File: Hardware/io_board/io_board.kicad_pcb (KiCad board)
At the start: 2 copper layers, 80.8 x 60.1 mm, 35 parts, among them J1 Conn_01x40, J2 Conn_02x06_Odd_Even, J3 Mini-DIN-6, J4 Conn_02x10_Odd_Even, J5 Conn_01x04_Male, U2 W65C22NxP, U3 74LS14, U4 74HC137

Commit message: update for kicad 6
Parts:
- removed the G*** at (39.9, -15.2)
- added G***: LOGO, Logo:logo, F.Cu at (40.3, -15.0)
- moved REF** 33.8 mm to (15.0, -12.3)
- moved REF** 1.17 mm to (8.55, -10.6)
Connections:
- J4 pad 13: unconnected-(J4-Pad13) -> GND
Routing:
- net GND: track 3.85 -> 7.18 mm
- net Net-(D2-Pad1): track 9.24 -> 6.87 mm
- net /PA0: track 43.2 -> 41.1 mm
- net ~{CONF}: track 68.5 -> 66.7 mm
- net /PA2: track 48.8 -> 47.1 mm
- net /PA4: track 49.0 -> 47.3 mm
- net /PA3: track 47.8 -> 46.5 mm
- net +5V: track 12.7 -> 11.9 mm
- net Net-(D8-Pad1): track 9.60 -> 8.84 mm
- net Net-(J3-Pad5): track 30.9 -> 30.1 mm
- net /PA5: track 51.5 -> 50.8 mm
- net ~{RESET}: track 31.3 -> 30.6 mm
- net /PA1: track 48.4 -> 47.8 mm
- net Net-(U3-Pad11): track 3.09 -> 2.54 mm
- net /SS4: track 9.85 -> 9.34 mm
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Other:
- board text added: "IO BOARD ${VERSION}"
- board text removed: "IO BOARD V1.1"
- board text removed: "IO BOARD V1.2"

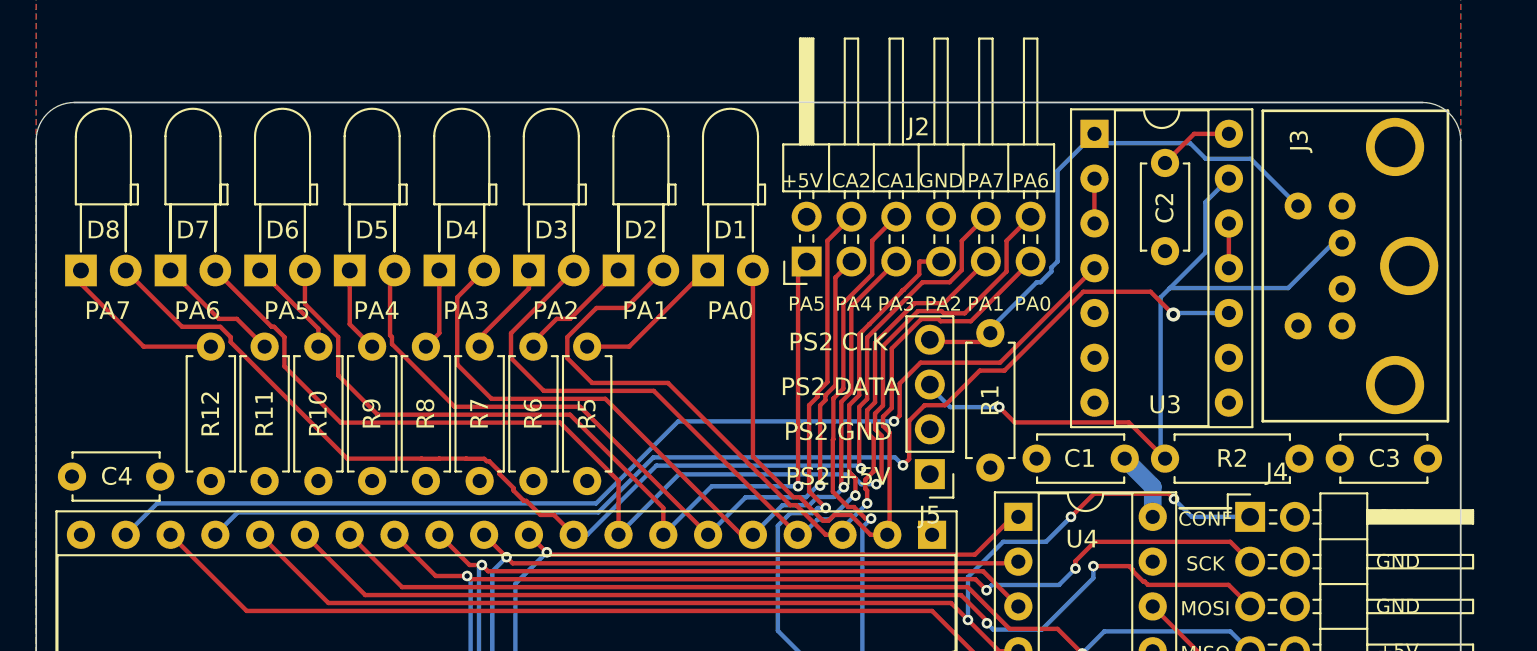
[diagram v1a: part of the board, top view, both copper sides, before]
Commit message: update io board
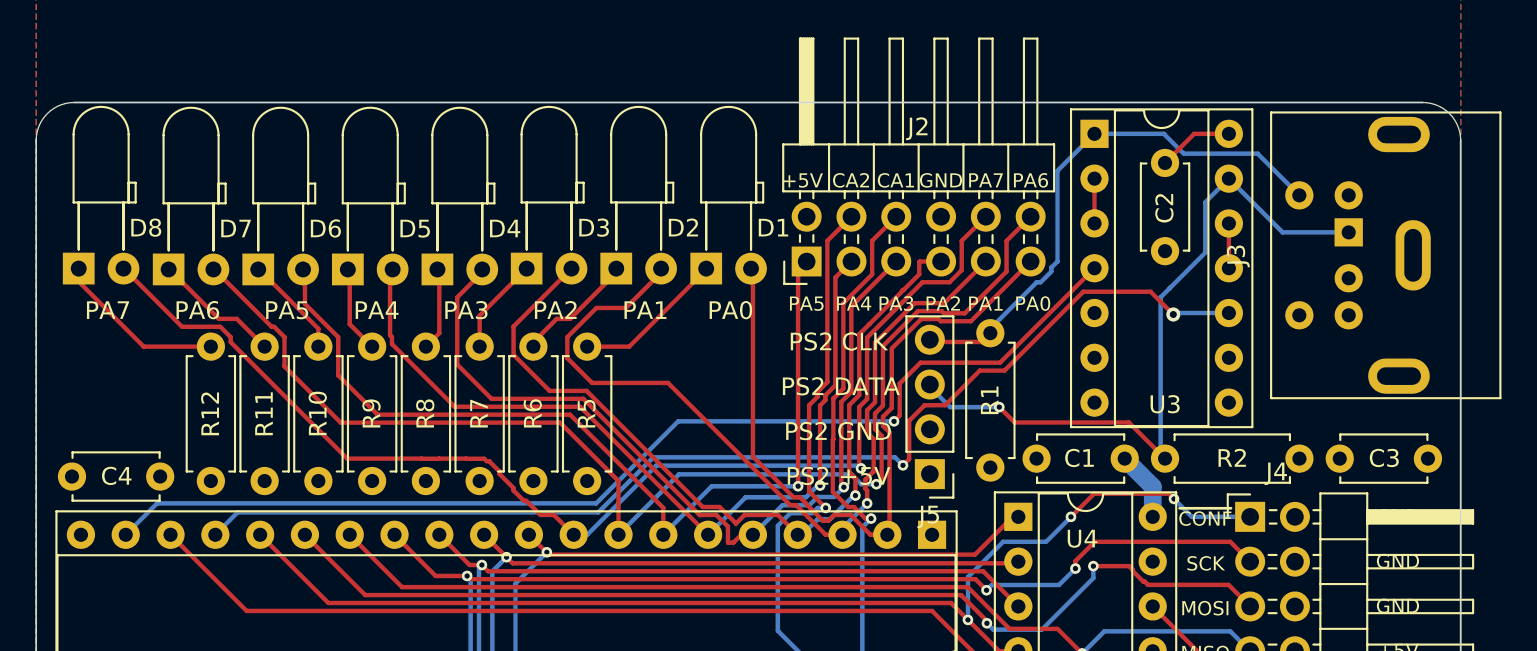
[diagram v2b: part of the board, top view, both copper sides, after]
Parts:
- D1, D2, D3, D4, D5, D6, D7, D8: footprint LED_THT:LED_D3.0mm_Horizontal_O3.81mm_Z6.0mm -> w_conn_av:LED_D3.0mm_Horizontal_O3.81mm_Z6.0mm_2
- J3: footprint mini-din:MINI-DIN-6-FULL-SHIELD -> Custom_Footprints:Connector_Mini-DIN_Female_6Pin_2rows
- moved D3 11.2 mm to (27.8, -60.5), turned to 0 degrees
- moved D1 11.2 mm to (38.0, -60.5), turned to 0 degrees
- moved D4 11.1 mm to (22.8, -60.4), turned to 0 degrees
- moved D8 10.3 mm to (2.41, -60.5), turned to 0 degrees
- moved D5 10.2 mm to (17.7, -60.4), turned to 0 degrees
- moved D7 10.2 mm to (7.51, -60.4), turned to 0 degrees
- moved D2 9.91 mm to (32.9, -60.5), turned to 0 degrees
- moved D6 9.86 mm to (12.6, -60.4), turned to 0 degrees
- moved J3 8.35 mm to (74.4, -52.7), turned to 90 degrees
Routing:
- net PS2_DATA: track 42.9 -> 40.6 mm
- net /PA3: track 46.5 -> 47.4 mm
- net Net-(J3-Pad5): track 30.1 -> 30.7 mm

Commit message: IO board DRC
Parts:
- moved C1 165.5 mm to (142.0, 104.9)
- moved C2 165.5 mm to (144.3, 88.1)
- moved C3 165.5 mm to (154.2, 104.9)
- moved C4 165.5 mm to (82.3, 105.9)
- moved D1 165.5 mm to (118.3, 84.3)
- moved D2 165.5 mm to (113.2, 84.3)
- moved D3 165.5 mm to (108.1, 84.3)
- moved D4 165.5 mm to (103.0, 84.4)
- moved D5 165.5 mm to (97.9, 84.4)
- moved D6 165.5 mm to (92.9, 84.4)
- moved D7 165.5 mm to (87.8, 84.4)
- moved D8 165.5 mm to (82.7, 84.3)
- moved G*** 165.5 mm to (120.5, 129.8)
- moved J1 165.5 mm to (158.5, 138.2)
- moved J2 165.5 mm to (124.0, 93.7)
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
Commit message: cleanup
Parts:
- moved REF** 3.30 mm to (98.6, 132.6)
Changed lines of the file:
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@@
   )
   (footprint "Symbol:OSHW-Logo2_7.3x6mm_SilkScreen" (layer "F.Cu")
-    (at 95.25 132.461)
+    (at 98.552 132.588)
     (descr "Open Source Hardware Symbol")
     (tags "Logo Symbol OSHW")

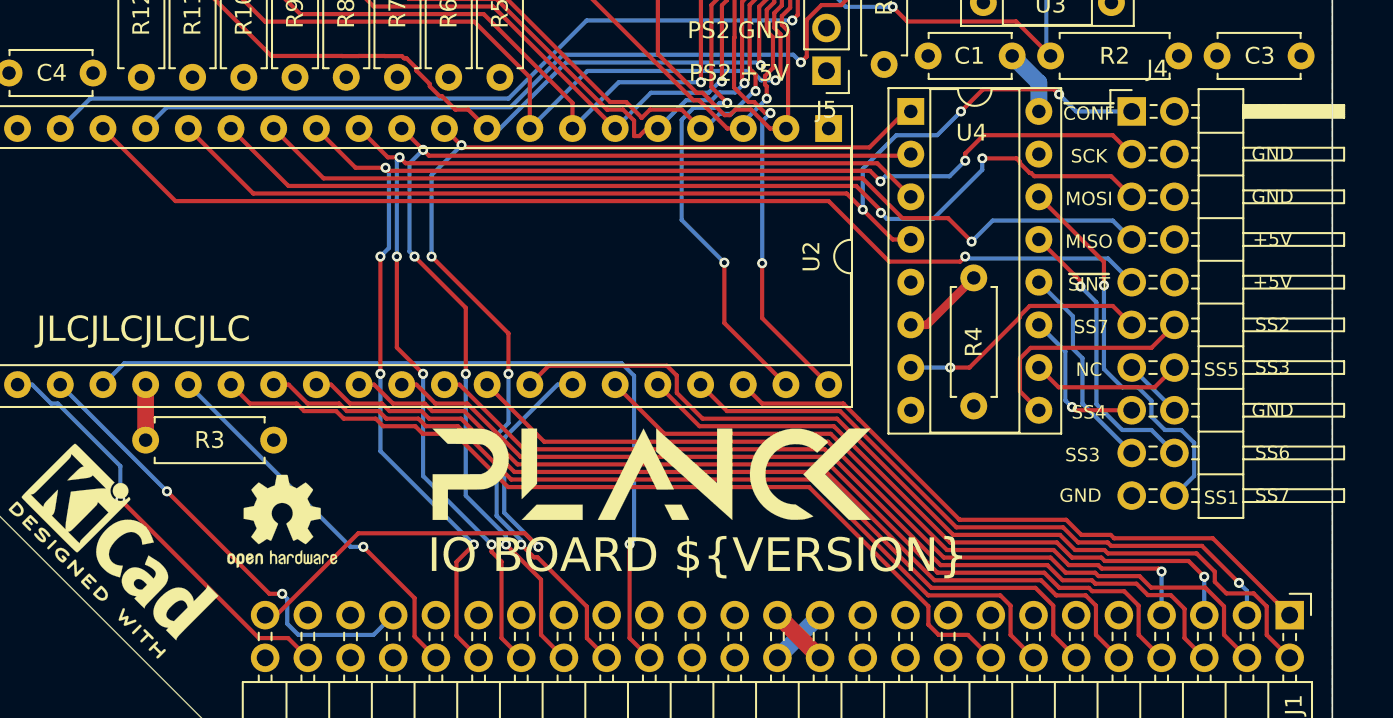
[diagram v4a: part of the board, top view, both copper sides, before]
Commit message: Can read file and list directories
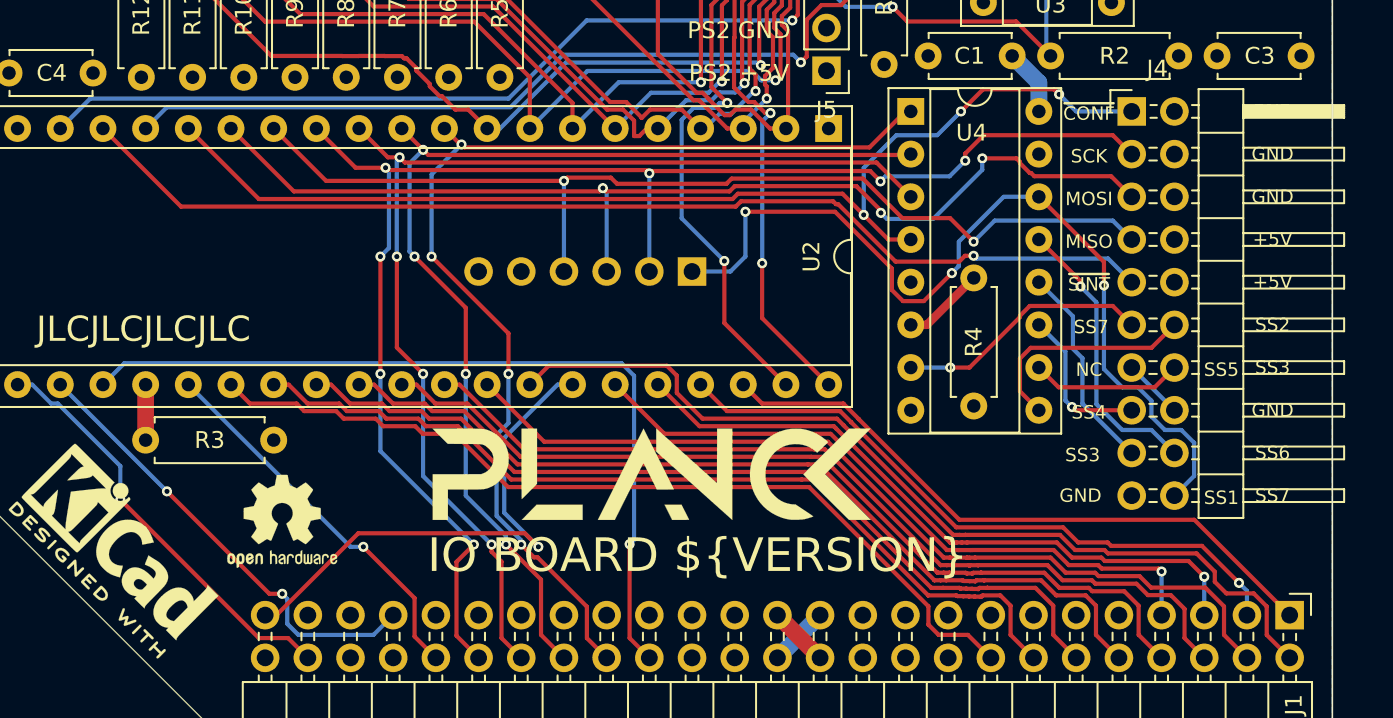
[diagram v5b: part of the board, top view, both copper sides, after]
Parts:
- added J6: Conn_01x06, Connector_PinSocket_2.54mm:PinSocket_1x06_P2.54mm_Vertical, B.Cu at (122.9, 117.7)
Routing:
- net /SS1: track 23.2 -> 53.3 mm, vias 1 -> 3
- net LED4: track 84.4 -> 90.4 mm, vias 6 -> 7
- net MISO: track 54.8 -> 60.6 mm, vias 1 -> 2
- net MOSI: track 58.6 -> 64.0 mm, vias 2 -> 3
- net ~{CONF}: track 66.7 -> 67.2 mm
